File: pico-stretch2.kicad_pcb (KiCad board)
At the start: 4 copper layers, 82.1 x 21 mm, 69 parts, among them J2 Conn_01x03_Pin, J4 Conn_01x64_Castellated_Pads, U1 RP2350B_C42415655, U3 ME6217C33M5G, U4 W25Q128JVSIQTR, U5 RPI Radio Module 2, U6 APS6404L-3SQR, X1 ABM8-272-T3_C20625731

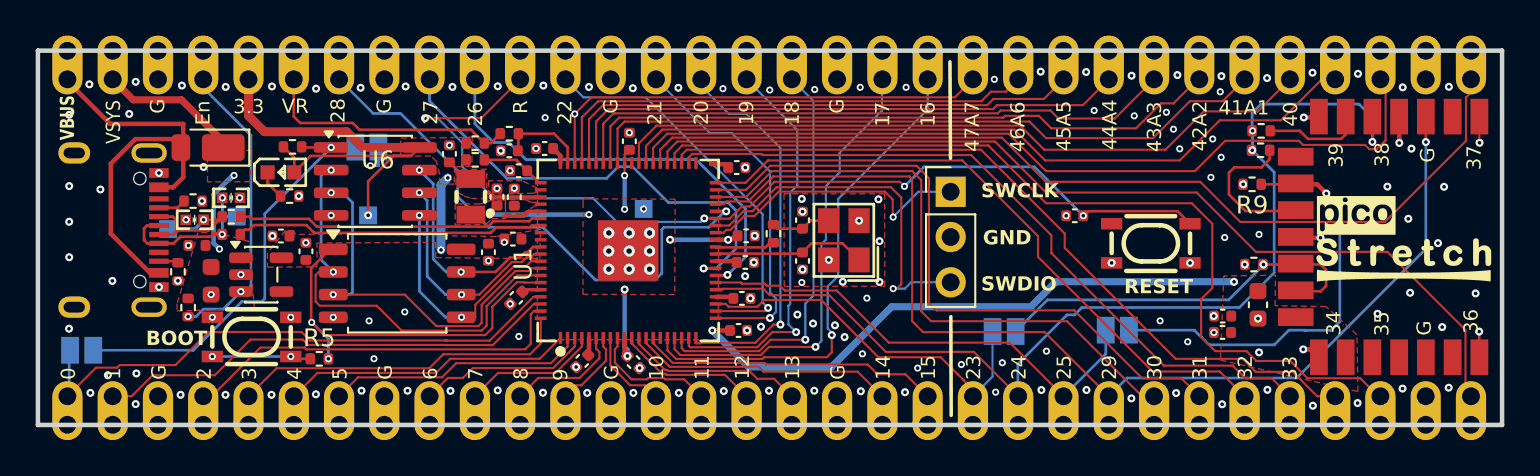
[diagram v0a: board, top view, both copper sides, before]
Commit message: Apply design review fixes and add re-review
Review 1 fixes (scripts/review_fixes.py, rebuilds from 54e971f):
- C9/C15 to 0402 C1525, R14 to 1k, C40 to 0603 10 uF with via-in-pad
- D3 in line on USB D+, C39 flipped to share D3 ground via
- C13 moved 0.05 mm clear of U1 pin 50
- Extended In1 VREG_LX cut-out, J4 pads 29-36 clipped
- U5 DNP with no paste, silkscreen fixes, named courtyard pairs
- VBUS TVS tried and removed

DESIGN_REVIEW_2.md and review2/ hold the re-review and its pack.
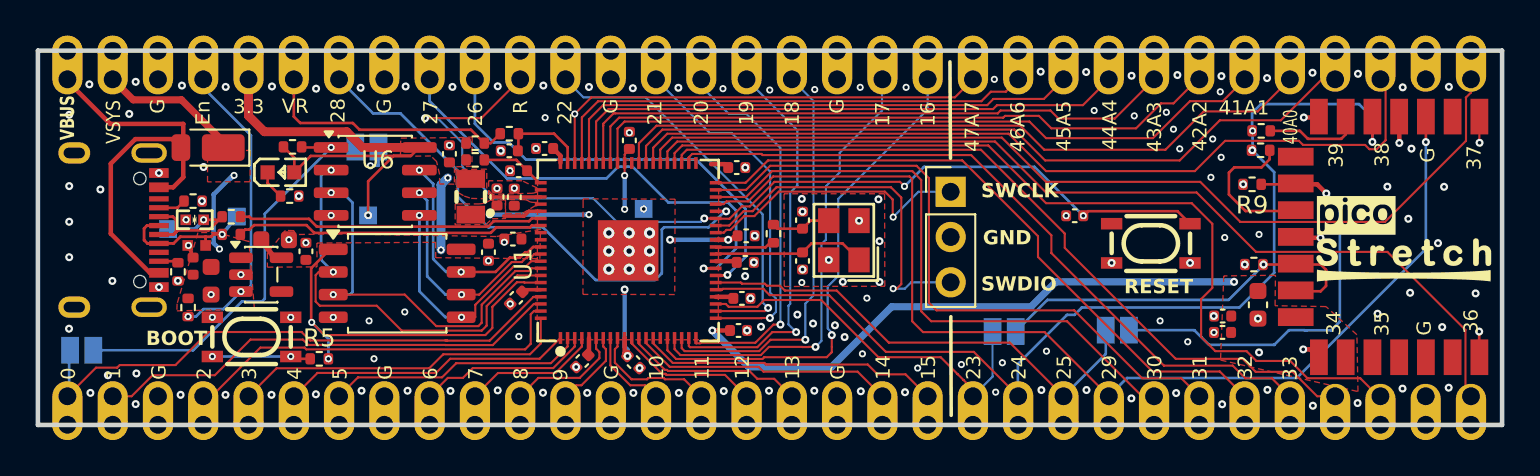
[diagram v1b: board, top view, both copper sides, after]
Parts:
- C40: value CL05A106MQ5NUNC -> 10uF; footprint Capacitor_SMD:C_0402_1005Metric -> Capacitor_SMD:C_0603_1608Metric
- R14: value 10kΩ -> 1kΩ
- moved D3 3.29 mm to (118.0, 101.9), turned to 0 degrees
- moved C39 1.18 mm to (117.8, 103.1), turned to 90 degrees
- moved C40 0.39 mm to (122.5, 101.6), turned to 180 degrees
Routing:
- net 3V3: track 70.0 -> 71.3 mm
- net USB2_D+: track 9.09 -> 8.01 mm, vias 2 -> 1
- net GND: track 7.68 -> 8.40 mm, vias 177 -> 176
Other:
- board text added: "40A0"
- board text removed: "40"

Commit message: Design review 3 fixes and Pico-footprint USB test pads
Review 3 (DESIGN_REVIEW_3.md, scripts/review3_fixes.py, from 1d4354a):
- 87 vias 0.4/0.2 -> 0.45/0.2 (JLC's free via); Default net class and
  DRC minimum via 0.45 mm; 0.45 mm via-to-plated-hole rule, hole_to_hole
  an error
- VREG_LX track 0.18 mm beside C10/C12 (JLC 0.1 mm pad-to-track)
- C2/C5 values swapped: 4.7 uF on DVDD pin 32, the pin furthest from
  the regulator (RP2350 datasheet 6.1.3)
- C9, RUN and GPIO47 vias moved off / into their own pads

USB test pads at the Pico 2's TP1-TP3 positions (scripts/pico_testpads.py),
so the board can be hot-plate soldered onto a Pico SMT footprint:
- TP3 (D-), TP4 (D+) and new TP5 (GND) on 1.5 x 1.5 mm R0.3 pads
  (Custom:TestPoint_Pad_1.5x1.5mm_R0.3mm), one new B.Cu stub each
- README: test pads and soldering onto a Pico footprint

review3/ holds the analysis packs, reviewer reports and via scripts.
production/ is still the pre-review output: regenerate before ordering.
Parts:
- added TP5: TestPoint, Custom:TestPoint_Pad_1.5x1.5mm_R0.3mm, B.Cu at (113.9, 101.5)
- C2: value 100nF -> 4.7uF
- C5: value 4.7uF -> 100nF
- TP3, TP4: footprint TestPoint:TestPoint_Pad_1.0x1.0mm -> Custom:TestPoint_Pad_1.5x1.5mm_R0.3mm
- moved TP4 9.91 mm to (110.6, 102.5)
- moved TP3 5.84 mm to (110.6, 100.5)
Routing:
- net USB2_D+: track 8.01 -> 17.7 mm
- net USB2_D-: track 9.22 -> 15.3 mm
- net GND: vias 176 -> 175
